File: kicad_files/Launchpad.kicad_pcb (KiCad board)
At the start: 2 copper layers, 76.2 x 119.7 mm, 174 parts, among them J1 TYPE-C-31-M12, J2 Conn_01x01, J3 Conn_02x05_Odd_Even, Q1 2N7002, Q2 AO3401A, SW1 SW_Push, SW10 Mechanical_Switch, SW11 Mechanical_Switch, SW12 Mechanical_Switch, SW13 Mechanical_Switch, SW14 Mechanical_Switch, SW15 Mechanical_Switch, SW16 Mechanical_Switch, SW17 Mechanical_Switch, SW18 Mechanical_Switch, SW19 Mechanical_Switch, SW2 RotaryEncoder_Switch, SW20 Mechanical_Switch, SW21 Mechanical_Switch, SW22 Mechanical_Switch, SW23 Mechanical_Switch, SW3 Mechanical_Switch, SW4 Mechanical_Switch, SW5 Mechanical_Switch, SW6 Mechanical_Switch, SW7 Mechanical_Switch, SW8 Mechanical_Switch, SW9 Mechanical_Switch, U1 TXS0101DBVR, U2 nRF52820-QDxx, U3 AP2112, U4 USBLC6-2SC6, X1 32MHz, X2 32.768kHz

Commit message: Removed submodule changes
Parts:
- D32, D33, D34, D35, D36, D37, D38, D39, D40, D41, D42, D45, D46, D47, D48, D49, D50, D52, D53, D54, D56: footprint acheron_Components:LED_SMD_0805 -> Launchpad:LED_SMD_0805
- SW22, SW23: footprint acheron_MXH_metalrings:MX200HVR -> Launchpad:MX200HVR

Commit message: V2 Changes
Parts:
- removed the C14 at (171.2, 58.9)
- removed the C22 at (171.5, 97.0)
- removed the C23 at (121.9, 58.3)
- removed the C29 at (152.4, 78.0)
- removed C35: 0.1uF, Capacitor_SMD:C_0805_2012Metric_Pad1.18x1.45mm_HandSolder
- removed the C9 at (113.1, 58.3)
- removed the D1 at (166.4, 58.3)
- removed the D25 at (147.3, 115.5)
- removed the D29 at (127.1, 139.0)
- removed the D3 at (166.4, 96.4)
- removed the D31 at (128.3, 58.3)
- removed the D6 at (147.3, 77.4)
- removed L2: 2.2nH, Inductor_SMD:L_0402_1005Metric
- removed the R11 at (173.6, 97.0)
- removed the R15 at (154.5, 78.0)
- removed the R17 at (154.5, 116.1)
- removed the R23 at (135.5, 58.9)
- removed the R5 at (174.3, 59.8)
- removed the U2 at (117.3, 116.6)
- added C32: 1uF, Capacitor_SMD:C_0805_2012Metric, F.Cu at (111.9, 58.3)
- added C8: 0.1uF, Capacitor_SMD:C_0603_1608Metric, F.Cu at (111.4, 118.1)
- added D27: D_Small, acheron_Components:D_SOD-123, F.Cu at (127.1, 100.3)
- added U1: nRF52840, Package_DFN_QFN:Nordic_AQFN-73-1EP_7x7mm_P0.5mm, F.Cu at (117.2, 116.6)
- C10: renamed from C15; footprint Capacitor_SMD:C_0805_2012Metric_Pad1.18x1.45mm_HandSolder -> Capacitor_SMD:C_0603_1608Metric
- C13: renamed from C18; footprint Capacitor_SMD:C_0805_2012Metric_Pad1.18x1.45mm_HandSolder -> Capacitor_SMD:C_0603_1608Metric
- C16, C27, C30, C31: footprint Capacitor_SMD:C_0805_2012Metric_Pad1.18x1.45mm_HandSolder -> Capacitor_SMD:C_0805_2012Metric
- C22: renamed from C28; footprint Capacitor_SMD:C_0805_2012Metric_Pad1.18x1.45mm_HandSolder -> Capacitor_SMD:C_0805_2012Metric
- C23: renamed from C36; footprint Capacitor_SMD:C_0805_2012Metric_Pad1.18x1.45mm_HandSolder -> Capacitor_SMD:C_0805_2012Metric
- C24: renamed from C20; footprint Capacitor_SMD:C_0805_2012Metric_Pad1.18x1.45mm_HandSolder -> Capacitor_SMD:C_0805_2012Metric
- C25: renamed from C32; footprint Capacitor_SMD:C_0805_2012Metric_Pad1.18x1.45mm_HandSolder -> Capacitor_SMD:C_0805_2012Metric
- C26: renamed from C37; footprint Capacitor_SMD:C_0805_2012Metric_Pad1.18x1.45mm_HandSolder -> Capacitor_SMD:C_0805_2012Metric
- C28: renamed from C34; footprint Capacitor_SMD:C_0805_2012Metric_Pad1.18x1.45mm_HandSolder -> Capacitor_SMD:C_0805_2012Metric
- C3: value 1pF -> 0.8pF
- C33: value 0.1uF -> 1uF; footprint Capacitor_SMD:C_0805_2012Metric_Pad1.18x1.45mm_HandSolder -> Capacitor_SMD:C_0805_2012Metric
- C4: value 1.2pF -> 0.5pF
- D29: renamed from D32; footprint Launchpad:LED_SMD_0805 -> LED_SMD:LED_0805_2012Metric_Pad1.15x1.40mm_HandSolder
- D30: renamed from D33; footprint Launchpad:LED_SMD_0805 -> LED_SMD:LED_0805_2012Metric_Pad1.15x1.40mm_HandSolder
- D31: renamed from D34; footprint Launchpad:LED_SMD_0805 -> LED_SMD:LED_0805_2012Metric_Pad1.15x1.40mm_HandSolder
- D32: renamed from D35; footprint Launchpad:LED_SMD_0805 -> LED_SMD:LED_0805_2012Metric_Pad1.15x1.40mm_HandSolder
- D33: renamed from D36; footprint Launchpad:LED_SMD_0805 -> LED_SMD:LED_0805_2012Metric_Pad1.15x1.40mm_HandSolder
- D34: renamed from D37; footprint Launchpad:LED_SMD_0805 -> LED_SMD:LED_0805_2012Metric_Pad1.15x1.40mm_HandSolder
- D35: renamed from D38; footprint Launchpad:LED_SMD_0805 -> LED_SMD:LED_0805_2012Metric_Pad1.15x1.40mm_HandSolder
- D36: renamed from D39; footprint Launchpad:LED_SMD_0805 -> LED_SMD:LED_0805_2012Metric_Pad1.15x1.40mm_HandSolder
- D37: renamed from D40; footprint Launchpad:LED_SMD_0805 -> LED_SMD:LED_0805_2012Metric_Pad1.15x1.40mm_HandSolder
- D38: renamed from D41; footprint Launchpad:LED_SMD_0805 -> LED_SMD:LED_0805_2012Metric_Pad1.15x1.40mm_HandSolder
- D39: renamed from D42; footprint Launchpad:LED_SMD_0805 -> LED_SMD:LED_0805_2012Metric_Pad1.15x1.40mm_HandSolder
- D40: renamed from D45; footprint Launchpad:LED_SMD_0805 -> LED_SMD:LED_0805_2012Metric_Pad1.15x1.40mm_HandSolder
- D41: renamed from D46; footprint Launchpad:LED_SMD_0805 -> LED_SMD:LED_0805_2012Metric_Pad1.15x1.40mm_HandSolder
- D42: renamed from D47; footprint Launchpad:LED_SMD_0805 -> LED_SMD:LED_0805_2012Metric_Pad1.15x1.40mm_HandSolder
- D43: renamed from D48; footprint Launchpad:LED_SMD_0805 -> LED_SMD:LED_0805_2012Metric_Pad1.15x1.40mm_HandSolder
- D44: renamed from D49; footprint Launchpad:LED_SMD_0805 -> LED_SMD:LED_0805_2012Metric_Pad1.15x1.40mm_HandSolder
- D45: renamed from D50; footprint Launchpad:LED_SMD_0805 -> LED_SMD:LED_0805_2012Metric_Pad1.15x1.40mm_HandSolder
- D46: renamed from D52; footprint Launchpad:LED_SMD_0805 -> LED_SMD:LED_0805_2012Metric_Pad1.15x1.40mm_HandSolder
- D47: renamed from D53; footprint Launchpad:LED_SMD_0805 -> LED_SMD:LED_0805_2012Metric_Pad1.15x1.40mm_HandSolder
- D48: renamed from D54; footprint Launchpad:LED_SMD_0805 -> LED_SMD:LED_0805_2012Metric_Pad1.15x1.40mm_HandSolder
- D49: renamed from D56; footprint Launchpad:LED_SMD_0805 -> LED_SMD:LED_0805_2012Metric_Pad1.15x1.40mm_HandSolder
- J2: footprint Connector_PinHeader_1.27mm:PinHeader_1x02_P1.27mm_Vertical -> Connector_PinHeader_2.00mm:PinHeader_1x02_P2.00mm_Vertical
- J3: footprint Connector_PinHeader_1.27mm:PinHeader_2x05_P1.27mm_Vertical -> Connector_PinHeader_1.27mm:PinHeader_2x05_P1.27mm_Vertical_SMD
- X1: footprint Crystal:Crystal_SMD_2012-2Pin_2.0x1.2mm_HandSoldering -> Crystal:Crystal_SMD_2520-4Pin_2.5x2.0mm
- moved C33 66.0 mm to (120.5, 58.3), turned to -90 degrees
- moved D28 37.5 mm to (127.1, 138.4)
- moved C2 6.11 mm to (122.9, 118.3), turned to 180 degrees
- moved C31 5.85 mm to (177.7, 59.0), turned to 180 degrees
- moved C30 5.85 mm to (174.0, 59.0), turned to 180 degrees
- moved C18 4.57 mm to (117.9, 108.5), turned to 90 degrees
- moved C17 3.92 mm to (119.9, 108.5), turned to 90 degrees
- moved C12 3.06 mm to (122.9, 116.8)
- moved C1 2.90 mm to (122.9, 123.4), turned to 0 degrees
- moved J3 2.65 mm to (119.3, 146.5)
- moved AE1 2.48 mm to (110.7, 135.0)
- moved X1 2.00 mm to (122.9, 120.9), turned to -90 degrees
- moved C15 1.82 mm to (118.7, 122.5)
- moved C11 1.82 mm to (120.2, 122.5)
- moved C7 1.49 mm to (111.4, 116.6)
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- renumbered C10 to C11, C11 to C12, C12 to C14, C13 to C15, C25 to C17, C26 to C18, C17 to C19, C19 to C20, C24 to C29, C8 to C9, D5 to D1, D9 to D10, D10 to D11, D11 to D12, D12 to D13, D44 to D2, D26 to D25, D27 to D26, D2 to D3, D13 to D4, D51 to D5, D4 to D6, D30 to D7, D7 to D8, D8 to D9, R14 to R10, R36 to R11, R8 to R12, R16 to R13, R43 to R14, R13 to R15, R18 to R16, R19 to R17, R20 to R18, R21 to R19, R22 to R20, R24 to R21, R25 to R22, R26 to R23, R27 to R24, R28 to R25, R29 to R26, R30 to R27, R31 to R28, R32 to R29, R33 to R30, R34 to R31, R37 to R32, R38 to R33, R39 to R34, R40 to R35, R41 to R36, R42 to R37, R44 to R38, R45 to R39, R46 to R40, R48 to R41, R7 to R5, R9 to R6, R6 to R7, R10 to R8, R12 to R9, U1 to U2
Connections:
- C33 pad 1: Net-(C33-Pad1) -> +3V3
- C4 pad 1: Net-(C4-Pad1) -> /RF
- D1 pad 2: Net-(D31-Pad4) -> /LED_5V
- D1 pad 4: Net-(D1-Pad2) -> Net-(D3-Pad4)
- D2 pad 4: Net-(D44-Pad4) -> Net-(D3-Pad2)
- D28 pad 1: ROW3 -> ROW5
- D3 pad 2: Net-(D2-Pad2) -> Net-(D3-Pad2)
- D3 pad 4: Net-(D1-Pad4) -> Net-(D3-Pad4)
- D4 pad 4: Net-(D13-Pad4) -> Net-(D4-Pad4)
- D5 pad 4: Net-(D25-Pad2) (its old number) -> Net-(D5-Pad4)
- D6 pad 2: Net-(D25-Pad4) -> Net-(D5-Pad4)
- D6 pad 4: Net-(D3-Pad4) -> Net-(D4-Pad4)
- J3 pad 9: GND -> unconnected-(J3-Pad9)
- L1 pad 2: Net-(C4-Pad1) -> /RF
- R21 pad 2: Net-(D32-PadA) -> Net-(R21-Pad2)
- R22 pad 2: Net-(D33-PadA) -> Net-(D30-Pad2)
- R23 pad 2: Net-(D34-PadA) -> Net-(R23-Pad2)
- R24 pad 2: Net-(D35-PadA) -> Net-(R24-Pad2)
- R25 pad 2: Net-(D36-PadA) -> Net-(R25-Pad2)
- R26 pad 2: Net-(D37-PadA) -> Net-(R26-Pad2)
- R27 pad 2: Net-(D38-PadA) -> Net-(R27-Pad2)
- R28 pad 2: Net-(D39-PadA) -> Net-(D36-Pad2)
- R29 pad 2: Net-(D40-PadA) -> Net-(R29-Pad2)
- R30 pad 2: Net-(D41-PadA) -> Net-(D38-Pad2)
- R31 pad 2: Net-(D42-PadA) -> Net-(R31-Pad2)
- R32 pad 2: Net-(D45-PadA) -> Net-(R32-Pad2)
- R33 pad 2: Net-(D46-PadA) -> Net-(R33-Pad2)
- R34 pad 2: Net-(D47-PadA) -> Net-(R34-Pad2)
- R35 pad 2: Net-(D48-PadA) -> Net-(D43-Pad2)
- R36 pad 2: Net-(D49-PadA) -> Net-(D44-Pad2)
- R37 pad 2: Net-(D50-PadA) -> Net-(R37-Pad2)
- R38 pad 1: Net-(D52-PadA) -> Net-(R38-Pad1)
- R39 pad 1: Net-(D53-PadA) -> Net-(D47-Pad2)
- R40 pad 1: Net-(D54-PadA) -> Net-(R40-Pad1)
- R41 pad 1: Net-(D56-PadA) -> Net-(R41-Pad1)
- SW22 pad 2: Net-(D28-Pad2) -> Net-(D27-Pad2)
- SW23 pad 2: Net-(D29-Pad2) -> Net-(D28-Pad2)
- X1 pad 2: Net-(C1-Pad2) -> GND
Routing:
- net Net-(D5-Pad4): track 0.00 -> 34.5 mm
- net Net-(D3-Pad2): track 0.00 -> 34.5 mm
- net Net-(D4-Pad4): track 0.00 -> 33.4 mm
- net COL3: track 139.6 -> 118.6 mm, vias 10 -> 8
- net Net-(D1-Pad4): track 20.8 -> 0.00 mm
- net ROW1: track 130.9 -> 147.6 mm
- net +3V3: track 190.5 -> 206.2 mm
- net /LED_5V: track 62.1 -> 77.7 mm
- net Net-(D31-Pad4): track 15.5 -> 0.00 mm
- net Net-(D25-Pad4): track 15.5 -> 0.00 mm
- net Net-(D25-Pad2) (its old number): track 15.5 -> 0.00 mm
- net Net-(D2-Pad2): track 15.5 -> 0.00 mm
- net Net-(D13-Pad4): track 15.5 -> 0.00 mm
- net Net-(D1-Pad2): track 15.5 -> 0.00 mm
- net Net-(D44-Pad4): track 15.5 -> 0.00 mm
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
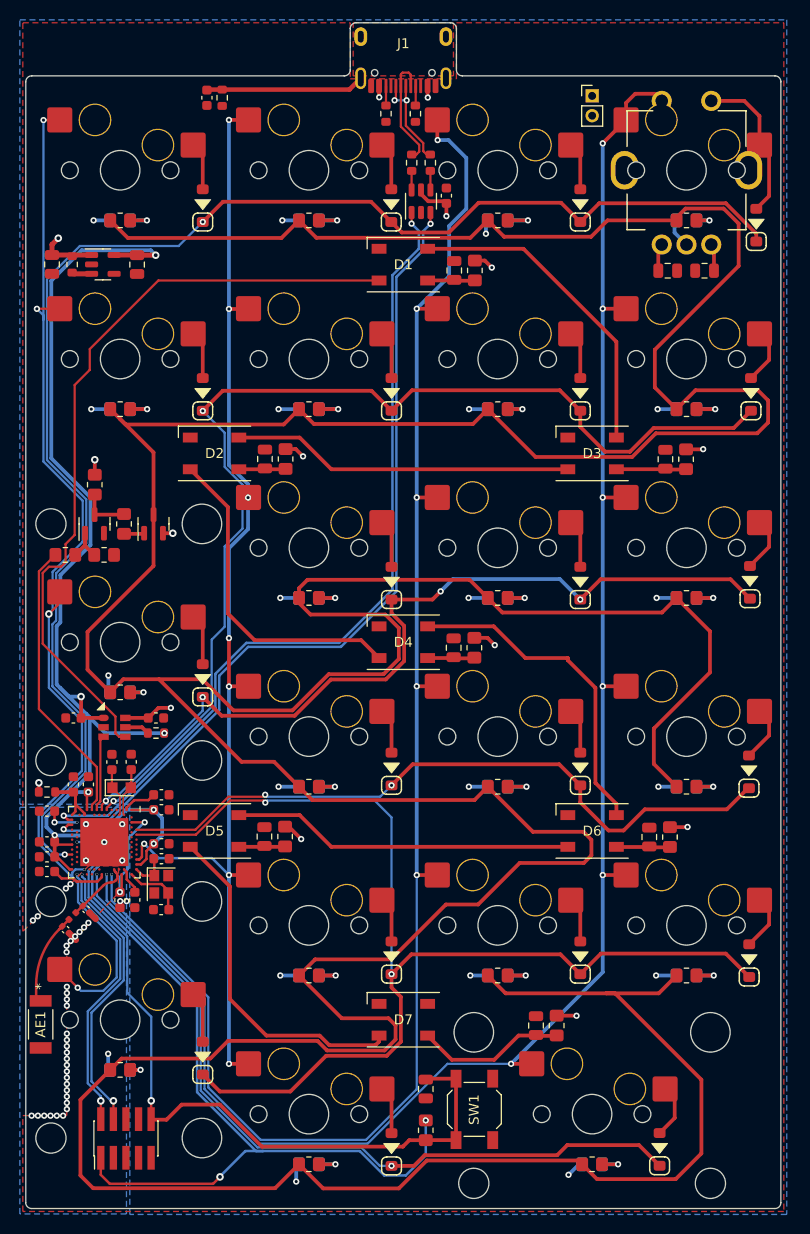
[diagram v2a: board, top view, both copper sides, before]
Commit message: Added Mini Launchpad
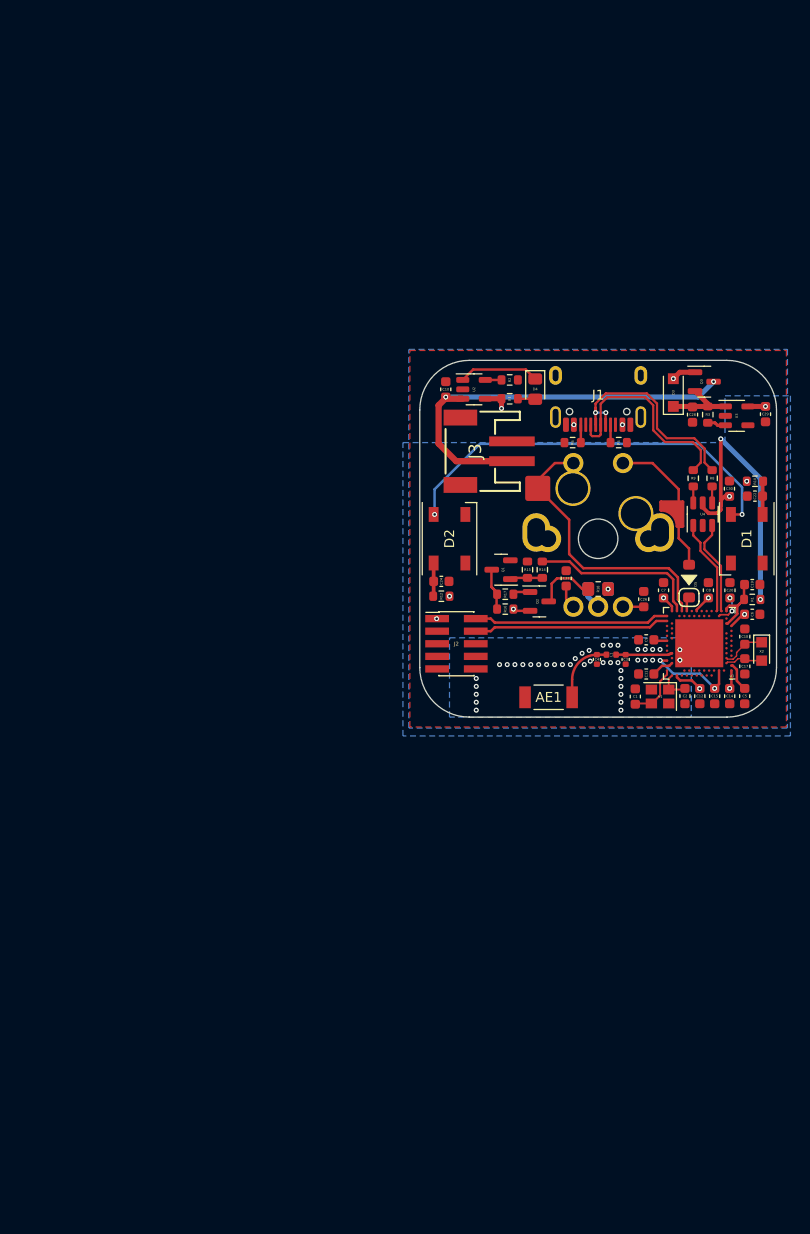
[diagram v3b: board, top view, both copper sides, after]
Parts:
- removed C13: 0.1uF, Capacitor_SMD:C_0603_1608Metric
- removed C16, C23, C25, C31: 0.1uF, Capacitor_SMD:C_0805_2012Metric
- removed C21: 4.7nF, Capacitor_SMD:C_0603_1608Metric
- removed C32, C33: 1uF, Capacitor_SMD:C_0805_2012Metric
- removed D10, D11, D12, D13, D14, D15, D16, D17, D18, D19, D20, D21, D22, D23, D24, D25, D26, D27, D28, D8, D9: D_Small, acheron_Components:D_SOD-123
- removed D29, D30, D31, D32, D33, D34, D35, D36, D37, D38, D39, D40, D41, D42, D43, D44, D45, D46, D47, D48, D49: LED, LED_SMD:LED_0805_2012Metric_Pad1.15x1.40mm_HandSolder
- removed D7: SK6812, LED_SMD:LED_SK6812_PLCC4_5.0x5.0mm_P3.2mm
- removed R11, R13: 5.1R, Resistor_SMD:R_0805_2012Metric_Pad1.20x1.40mm_HandSolder
- removed R19: 10K, Resistor_SMD:R_0805_2012Metric_Pad1.20x1.40mm_HandSolder
- removed R20: 100, Resistor_SMD:R_0805_2012Metric_Pad1.20x1.40mm_HandSolder
- removed R21, R22, R23, R24, R25, R26, R27, R28, R29, R30, R31, R32, R33, R34, R35, R36, R37, R38, R39, R40, R41: 1K, Resistor_SMD:R_0805_2012Metric_Pad1.20x1.40mm_HandSolder
- removed R7: 1M, Resistor_SMD:R_0603_1608Metric
- removed SW1: SW_Push, acheron_Hardware:K2-1187SQ-A4SW-06
- removed SW10, SW11, SW12, SW13, SW14, SW15, SW16, SW17, SW18, SW19, SW20, SW21, SW3, SW4, SW5, SW6, SW7, SW9: Mechanical_Switch, acheron_MXH_metalrings:MX100H
- removed SW22, SW23: Mechanical_Switch, Launchpad:MX200HVR
- removed SW8: Mechanical_Switch, acheron_MXH_metalrings:MX200HR
- added Q3: AO3401A, Package_TO_SOT_SMD:SOT-23, F.Cu at (177.7, 70.2)
- C10: value 0.1uF -> 10uF
- C22, C24, C26, C27, C30: footprint Capacitor_SMD:C_0805_2012Metric -> Capacitor_SMD:C_0603_1608Metric
- C28: value 0.1uF -> 10uF; footprint Capacitor_SMD:C_0805_2012Metric -> Capacitor_SMD:C_0603_1608Metric
- C29: value 0.1uF -> 1uF
- D3: value SK6812 -> D_Schottky_Small; footprint LED_SMD:LED_SK6812_PLCC4_5.0x5.0mm_P3.2mm -> Diode_SMD:D_SOD-123F
- D4: value SK6812 -> Orange; footprint LED_SMD:LED_SK6812_PLCC4_5.0x5.0mm_P3.2mm -> LED_SMD:LED_0805_2012Metric_Pad1.15x1.40mm_HandSolder
- D5: value SK6812 -> D_Small; footprint LED_SMD:LED_SK6812_PLCC4_5.0x5.0mm_P3.2mm -> acheron_Components:D_SOD-123
- D6: value SK6812 -> LED; footprint LED_SMD:LED_SK6812_PLCC4_5.0x5.0mm_P3.2mm -> LED_SMD:LED_0805_2012Metric_Pad1.15x1.40mm_HandSolder; moved to B.Cu
- J2: value Conn_01x01 -> Conn_02x05_Odd_Even; footprint Connector_PinHeader_2.00mm:PinHeader_1x02_P2.00mm_Vertical -> Connector_PinHeader_1.27mm:PinHeader_2x05_P1.27mm_Vertical_SMD
- J3: value Conn_02x05_Odd_Even -> Conn_01x02; footprint Connector_PinHeader_1.27mm:PinHeader_2x05_P1.27mm_Vertical_SMD -> Launchpad:JSTPH2
- R10, R12, R17: footprint Resistor_SMD:R_0805_2012Metric_Pad1.20x1.40mm_HandSolder -> Resistor_SMD:R_0603_1608Metric
- R14: value 5.1R -> 100; footprint Resistor_SMD:R_0805_2012Metric_Pad1.20x1.40mm_HandSolder -> Resistor_SMD:R_0603_1608Metric
- R15, R16: value 5.1R -> 10K; footprint Resistor_SMD:R_0805_2012Metric_Pad1.20x1.40mm_HandSolder -> Resistor_SMD:R_0603_1608Metric
- R18: value 10K -> 1K
- R4: value 10K -> 1K; footprint Resistor_SMD:R_0805_2012Metric_Pad1.20x1.40mm_HandSolder -> Resistor_SMD:R_0603_1608Metric
- SW2: footprint acheron_Hardware:ALPS_EC11E -> Launchpad:ALPS_EC11E
- U2: value TXS0101DBVR -> MCP73831-2-OT; footprint acheron_Components:SOT-23-6 -> Package_TO_SOT_SMD:SOT-23-5
- moved J3 77.8 mm to (154.6, 77.2)
- moved R4 74.3 mm to (158.1, 71.9), turned to 180 degrees
- moved R1 73.8 mm to (182.6, 92.1), turned to 180 degrees
- moved C20 72.4 mm to (180.3, 91.2), turned to 90 degrees
- moved C8 72.0 mm to (178.1, 91.2), turned to 90 degrees
- moved C19 71.4 mm to (182.6, 90.6), turned to 0 degrees
- moved C6 69.2 mm to (182.6, 93.6), turned to 0 degrees
- moved C7 67.2 mm to (173.6, 91.2), turned to 90 degrees
- moved X2 66.0 mm to (183.5, 97.4), turned to -90 degrees
- moved R3 65.9 mm to (178.1, 73.5)
- moved U3 65.8 mm to (181.0, 73.6)
- moved C18 65.1 mm to (181.8, 95.9)
- moved C9 64.8 mm to (171.8, 96.2)
- moved C28 63.6 mm to (176.5, 73.5), turned to -90 degrees
- moved C15 63.4 mm to (178.8, 101.9)
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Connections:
- C10 pad 1: GND -> VBAT
- C10 pad 2: +3V3 -> GND
- C24 pad 1: Net-(D3-Pad3) -> Net-(C24-Pad1)
- C26 pad 1: Net-(D5-Pad3) -> E_B
- C27 pad 1: Net-(D6-Pad3) -> GND
- C27 pad 2: GND -> E_A
- C28 pad 1: Net-(D7-Pad3) -> Net-(C28-Pad1)
- C29 pad 1: GND -> +3V3
- C29 pad 2: VBUS -> GND
- C30 pad 2: E_A -> VBUS
- D1 pad 2: /LED_5V -> /LED_3.3V
- D1 pad 4: Net-(D3-Pad4) -> Net-(D1-Pad4)
- D2 pad 2: Net-(D4-Pad2) -> Net-(D1-Pad4)
- D2 pad 3: Net-(D2-Pad3) -> Net-(C24-Pad1)
- D2 pad 4: Net-(D3-Pad2) -> unconnected-(D2-Pad4)
- D3 pad 1: GND -> Net-(C28-Pad1)
- D3 pad 2: Net-(D3-Pad2) -> VBUS
- D4 pad 1: GND -> Net-(D4-Pad1)
- D5 pad 1: GND -> ROW1
- D5 pad 2: Net-(D7-Pad2) -> S2
- D6 pad 2: Net-(D5-Pad4) -> Net-(D6-Pad2)
- J1 pad S1: /SHIELD -> GND
- J2 pad 1: VBUS -> +3V3
- J2 pad 2: GND -> /SWDIO
- J3 pad 1: +3V3 -> VBAT
- J3 pad 2: /SWDIO -> GND
- Q2 pad 2: VBUS -> +3V3
- R10 pad 2: VBUS -> +3V3
- R12 pad 1: Net-(D3-Pad3) -> Net-(C24-Pad1)
- R12 pad 2: VBUS -> +3V3
- R14 pad 1: Net-(D5-Pad3) -> /BKLT
- R14 pad 2: VBUS -> Net-(Q1-Pad1)
- R15 pad 1: Net-(D6-Pad3) -> GND
- R15 pad 2: VBUS -> Net-(Q1-Pad1)
- R16 pad 1: Net-(D7-Pad3) -> Net-(Q1-Pad3)
- R16 pad 2: VBUS -> +3V3
- R17 pad 1: /BKLT -> Net-(Q2-Pad1)
- R17 pad 2: Net-(Q1-Pad1) -> Net-(Q1-Pad3)
- R18 pad 1: GND -> Net-(Q2-Pad3)
- R18 pad 2: Net-(Q1-Pad1) -> Net-(D6-Pad2)
- R2 pad 1: +3V3 -> GND
- R3 pad 1: VBUS -> Net-(C28-Pad1)
- R4 pad 1: +3V3 -> Net-(D4-Pad2)
- R4 pad 2: /RESET -> VBUS
- U1 pad A10: ROW5 -> unconnected-(U1-PadA10)
- U1 pad A20: COL3 -> unconnected-(U1-PadA20)
- U1 pad A8: ROW4 -> unconnected-(U1-PadA8)
- U1 pad AD20: unconnected-(U1-PadAD20) -> COL1
- U1 pad AD22: unconnected-(U1-PadAD22) -> /BKLT
- U1 pad J24: COL2 -> unconnected-(U1-PadJ24)
- U1 pad L1: ROW2 -> unconnected-(U1-PadL1)
- U1 pad L24: COL1 -> unconnected-(U1-PadL24)
- U1 pad N1: ROW3 -> unconnected-(U1-PadN1)
- U1 pad R24: ROW6 -> unconnected-(U1-PadR24)
- U1 pad U1: /BKLT -> unconnected-(U1-PadU1)
- U1 pad Y23: COL4 -> unconnected-(U1-PadY23)
- U2 pad 1: +3V3 -> Net-(D4-Pad1)
- U2 pad 3: /LED_3V3 -> VBAT
- U2 pad 4: /LED_5V -> VBUS
- U3 pad 1: VBUS -> Net-(C28-Pad1)
- U4 pad 1: D- -> D+
- U4 pad 3: D+ -> D-
- U4 pad 4: /DP -> /DN
- U4 pad 6: /DN -> /DP
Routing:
- net Net-(Q2-Pad3): track 575.1 -> 6.14 mm
- net +3V3: track 206.2 -> 13.8 mm, vias 9 -> 10
- net COL2: track 160.9 -> 0.00 mm, vias 6 -> 0
- net COL1: track 179.8 -> 28.6 mm, vias 7 -> 0
- net ROW1: track 147.6 -> 1.47 mm, vias 2 -> 0
- net COL3: track 118.6 -> 0.00 mm, vias 8 -> 0
- net ROW5: track 113.4 -> 0.00 mm, vias 2 -> 0
- net COL4: track 112.3 -> 0.00 mm, vias 5 -> 0
- net ROW2: track 110.9 -> 0.00 mm, vias 2 -> 0
- net ROW3: track 85.7 -> 0.00 mm, vias 4 -> 0
- net /LED_5V: track 77.7 -> 0.00 mm
- net ROW6: track 77.4 -> 0.00 mm, vias 2 -> 0
- net D+: track 86.4 -> 9.66 mm, vias 2 -> 0
- net D-: track 85.1 -> 9.67 mm, vias 2 -> 0
- net /RESET: track 74.7 -> 0.00 mm, vias 2 -> 0
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- added copper zone on B.Cu, net +3V3
- removed copper zone on F.Cu, net /SHIELD
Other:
- board size 76.2 x 119.7 mm -> 36 x 36 mm
